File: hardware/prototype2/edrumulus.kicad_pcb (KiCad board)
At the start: 2 copper layers, 82 parts, among them J1 NMJ6HCD2, J10 DIN-5, J2 NMJ6HCD2, J3 NMJ6HCD2, J4 NMJ6HCD2, J5 NMJ6HCD2, J6 NMJ6HCD2, J7 NMJ6HCD2, J8 NMJ6HCD2, J9 NMJ6HCD2, U1 ESP32-DEVKIT-V1, U2 6N138

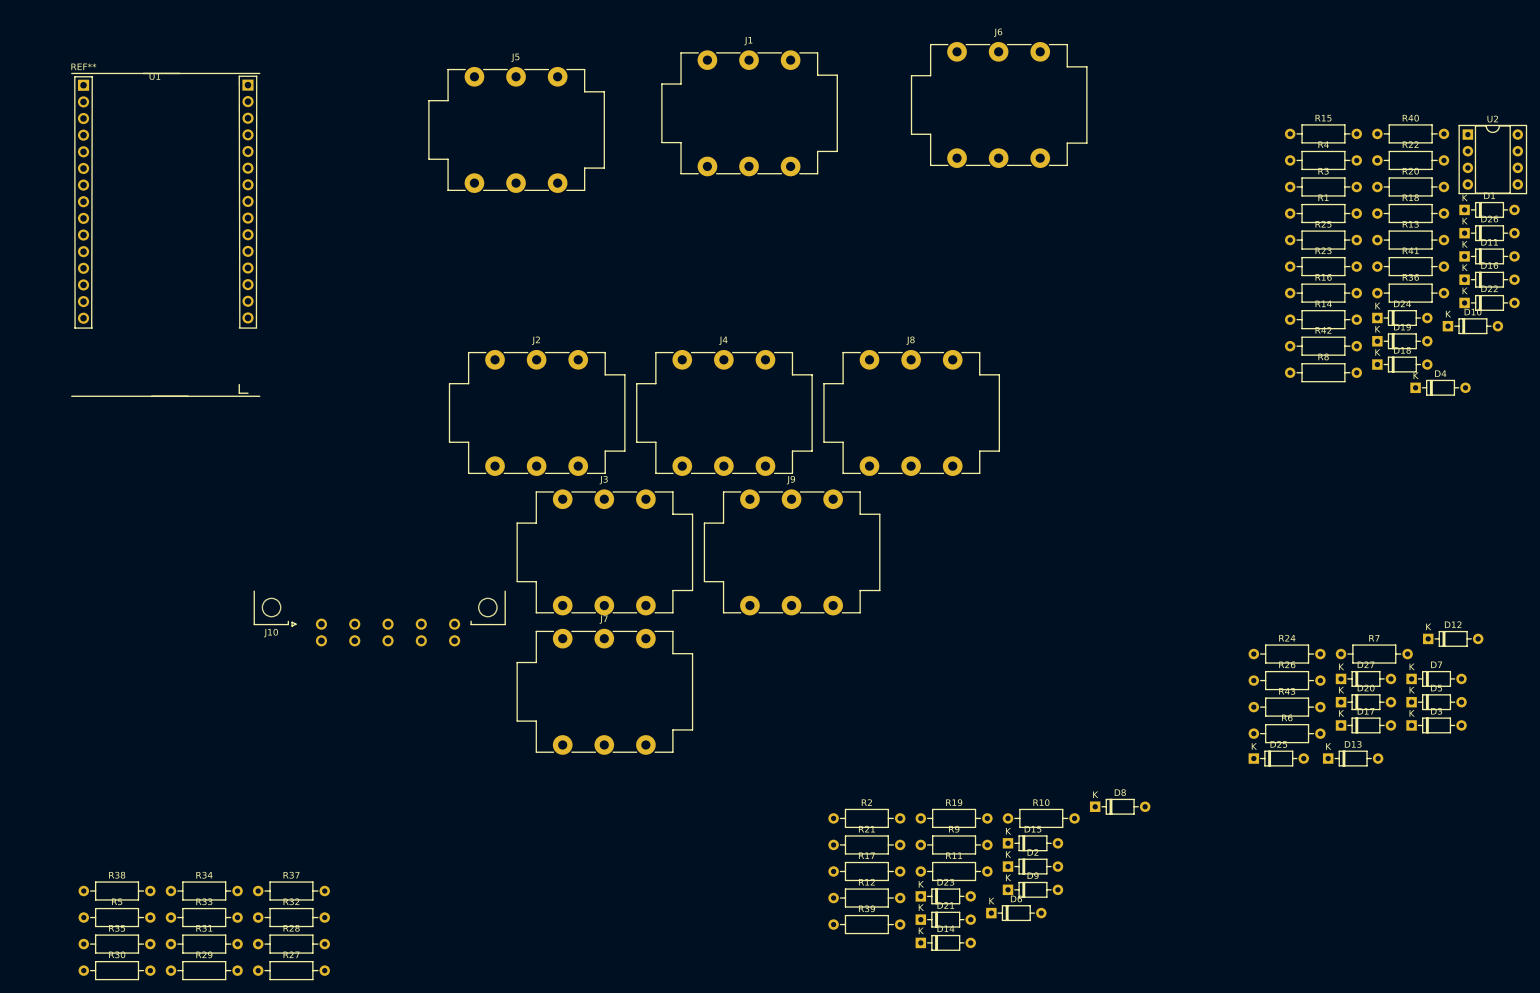
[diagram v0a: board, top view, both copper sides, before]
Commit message: fix bug with MIDI IN/OUT
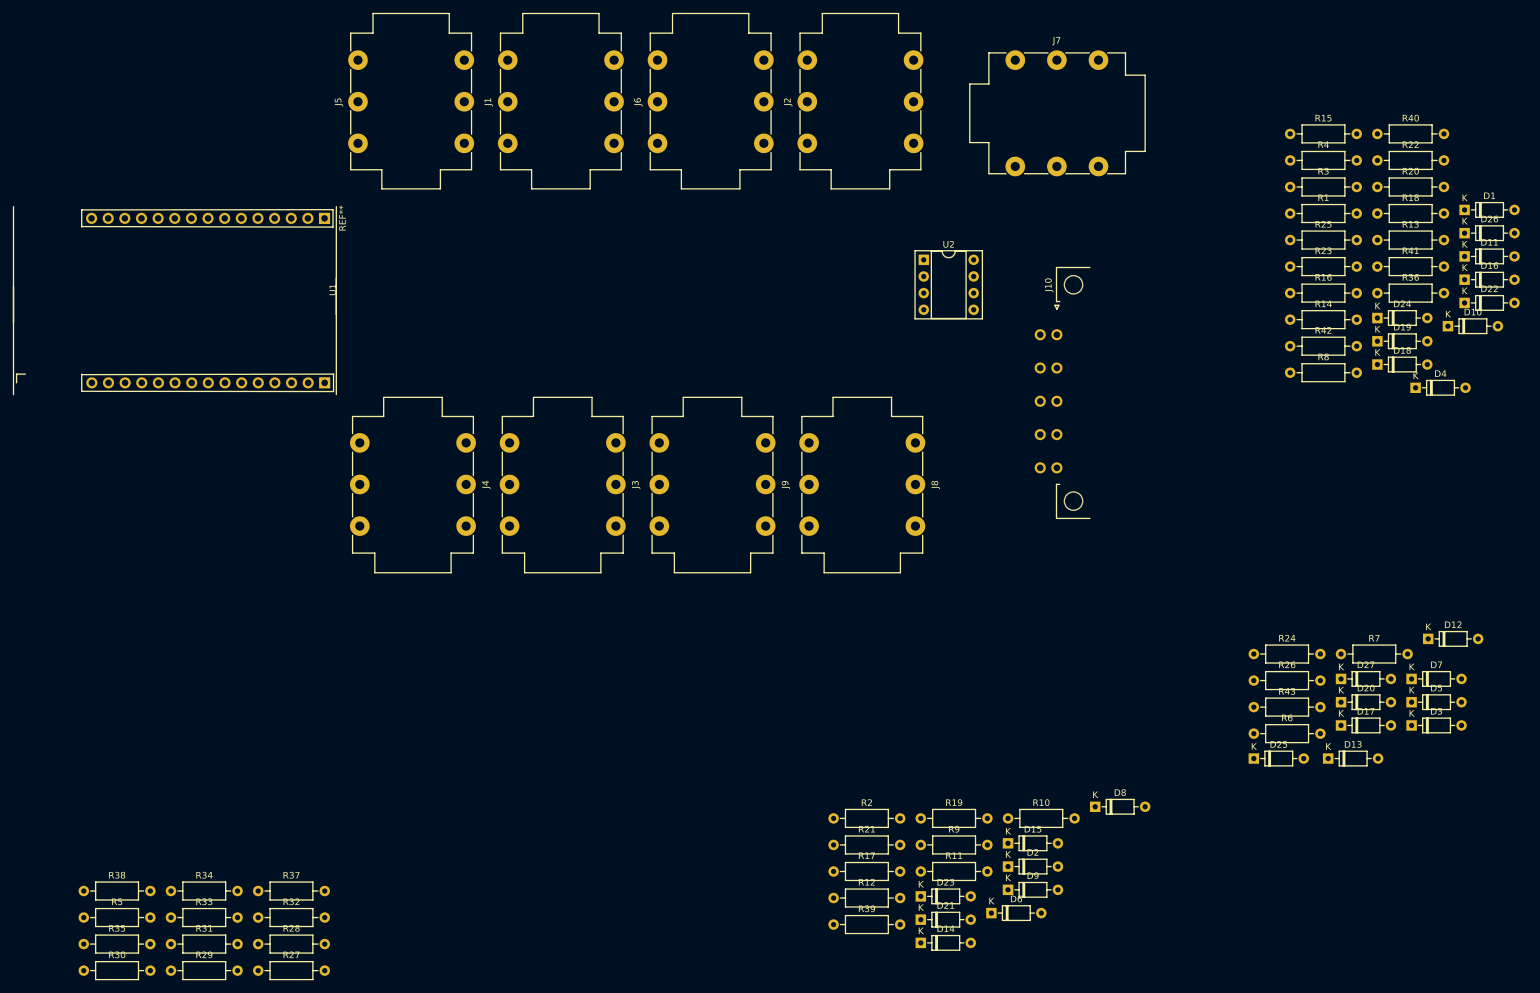
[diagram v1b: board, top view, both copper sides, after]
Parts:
- moved J10 123.9 mm to (194.3, 69.8), turned to 270 degrees
- moved J7 112.1 mm to (188.0, 30.5)
- moved U2 85.2 mm to (174.0, 61.0)
- moved J2 58.0 mm to (156.2, 43.2), turned to 90 degrees
- moved J6 47.8 mm to (133.3, 43.2), turned to 90 degrees
- moved U1 42.1 mm to (82.5, 54.6), turned to 270 degrees
- moved J4 35.3 mm to (104.1, 88.9), turned to 270 degrees
- moved J1 33.0 mm to (110.5, 43.2), turned to 90 degrees
- moved J5 20.5 mm to (87.6, 43.2), turned to 90 degrees
- moved J8 14.5 mm to (172.7, 88.9), turned to 270 degrees
- moved J3 11.8 mm to (127.0, 88.9), turned to 270 degrees
- moved J9 8.93 mm to (149.9, 88.9), turned to 270 degrees

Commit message: some updated to PCB
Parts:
- added J11: DIN-5, Connector_DIN:DIN41612_B3_2x5_Horizontal, F.Cu at (208.3, 74.9)
- moved J10 40.6 mm to (208.3, 31.8)
- moved U2 22.2 mm to (185.4, 80.0)
- moved J7 15.5 mm to (179.1, 43.2), turned to 90 degrees
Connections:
- R39 pad 1: Net-(J10-Pad4) -> Net-(D27-Pad1)
- R39 pad 2: Net-(D27-Pad1) -> Net-(J10-Pad4)
- R41 pad 1: UART_TX -> Net-(J11-Pad5)
- R41 pad 2: Net-(J10-Pad2) -> UART_TX

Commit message: reorder jack sockets
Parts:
- J1: value NMJ6HCD2 -> Snare
- J2: value NMJ6HCD2 -> Hi-Hat
- J3: value NMJ6HCD2 -> Crash
- J4: value NMJ6HCD2 -> Ride
- J5: value NMJ6HCD2 -> Kick
- J6: value NMJ6HCD2 -> Tom1
- J7: value NMJ6HCD2 -> Tom2
- J8: value NMJ6HCD2 -> Tom3
- J9: value NMJ6HCD2 -> Hi-Hat Ctrl
- moved J6 49.8 mm to (149.9, 90.2), turned to 270 degrees
- moved J7 47.4 mm to (172.7, 90.2), turned to 270 degrees
- moved J9 46.2 mm to (156.2, 43.2), turned to 90 degrees
- moved U2 42.4 mm to (191.8, 38.1), turned to 180 degrees
- moved J8 22.9 mm to (195.6, 90.2)
- moved J3 22.9 mm to (104.1, 90.2)
- moved J4 22.9 mm to (127.0, 90.2)
- moved J2 22.9 mm to (133.3, 43.2)
- moved J1 22.9 mm to (87.6, 43.2)
- moved J5 22.9 mm to (110.5, 43.2)

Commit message: some tests, moving components
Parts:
- moved R38 167.5 mm to (179.1, 55.9), turned to 180 degrees
- moved R28 151.3 mm to (195.6, 77.5), turned to 90 degrees
- moved R39 137.6 mm to (199.4, 30.5), turned to 270 degrees
- moved R12 136.4 mm to (64.8, 61.0)
- moved R27 136.1 mm to (172.7, 77.5), turned to 90 degrees
- moved R31 135.0 mm to (54.6, 30.5)
- moved R30 132.7 mm to (77.5, 40.6), turned to 90 degrees
- moved R10 132.3 mm to (91.4, 54.6)
- moved R37 130.0 mm to (153.7, 55.9)
- moved R29 129.4 mm to (71.1, 40.6), turned to 90 degrees
- moved R11 125.3 mm to (91.4, 59.7)
- moved R21 114.6 mm to (76.2, 72.4)
- moved R35 104.4 mm to (44.5, 61.0)
- moved R17 101.3 mm to (184.2, 55.9)
- moved R5 101.1 mm to (104.1, 78.7), turned to 180 degrees
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
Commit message: small fixes
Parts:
- removed J10, J11: DIN-5, Connector_DIN:DIN41612_B3_2x5_Horizontal

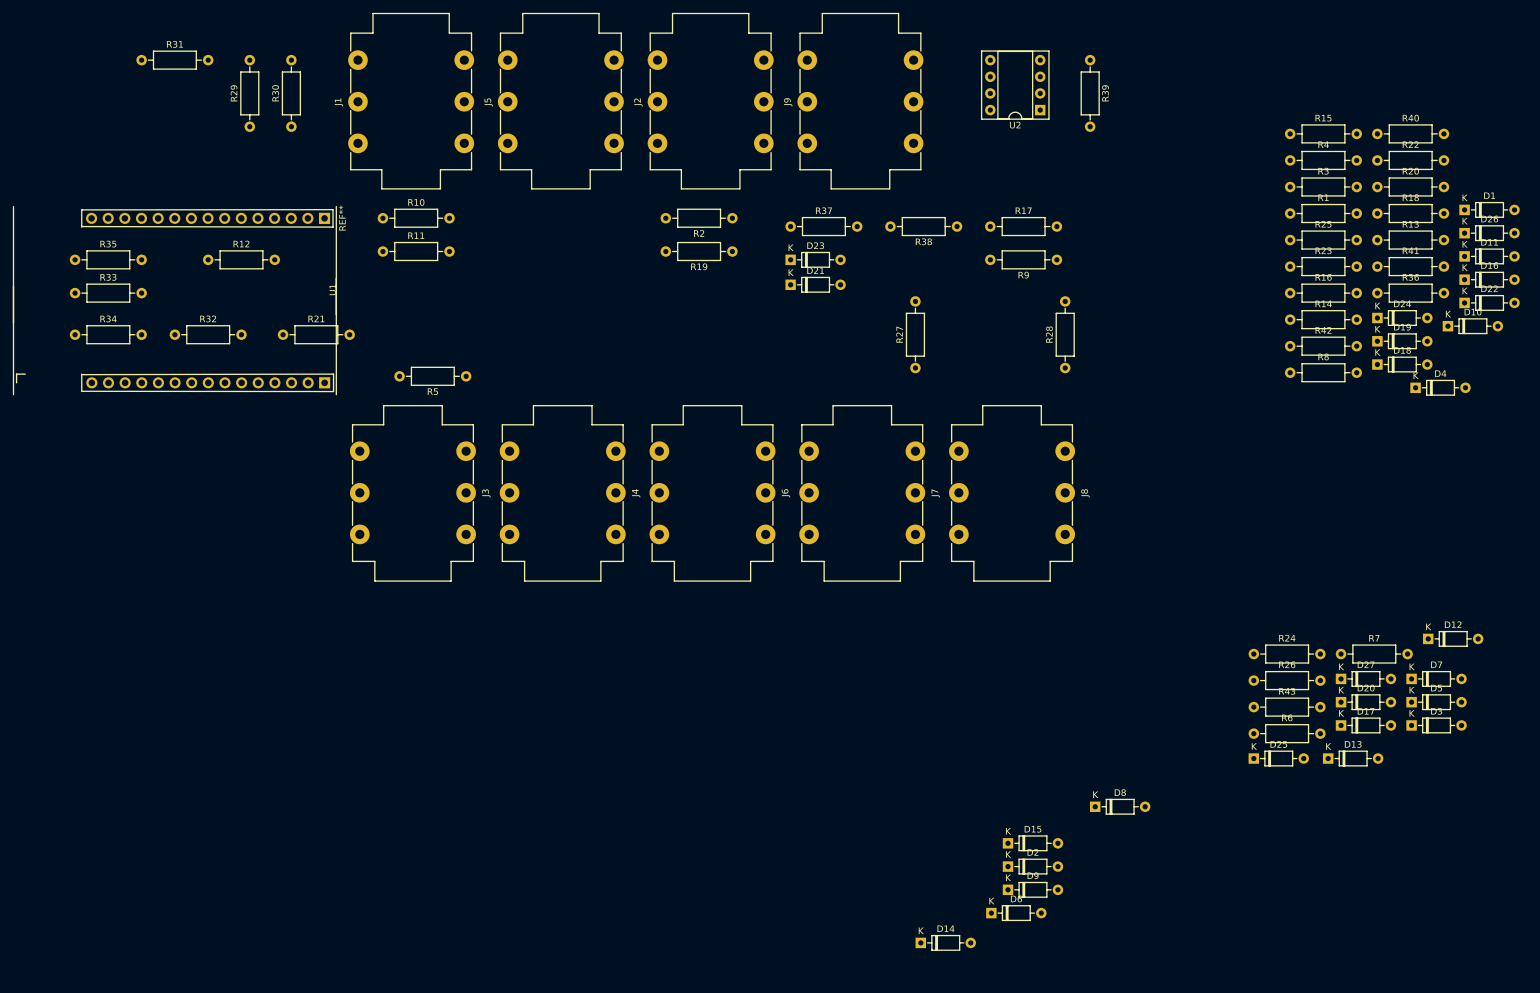
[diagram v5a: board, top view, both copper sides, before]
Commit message: clean up schematics -> PCB must be re-started from scratch
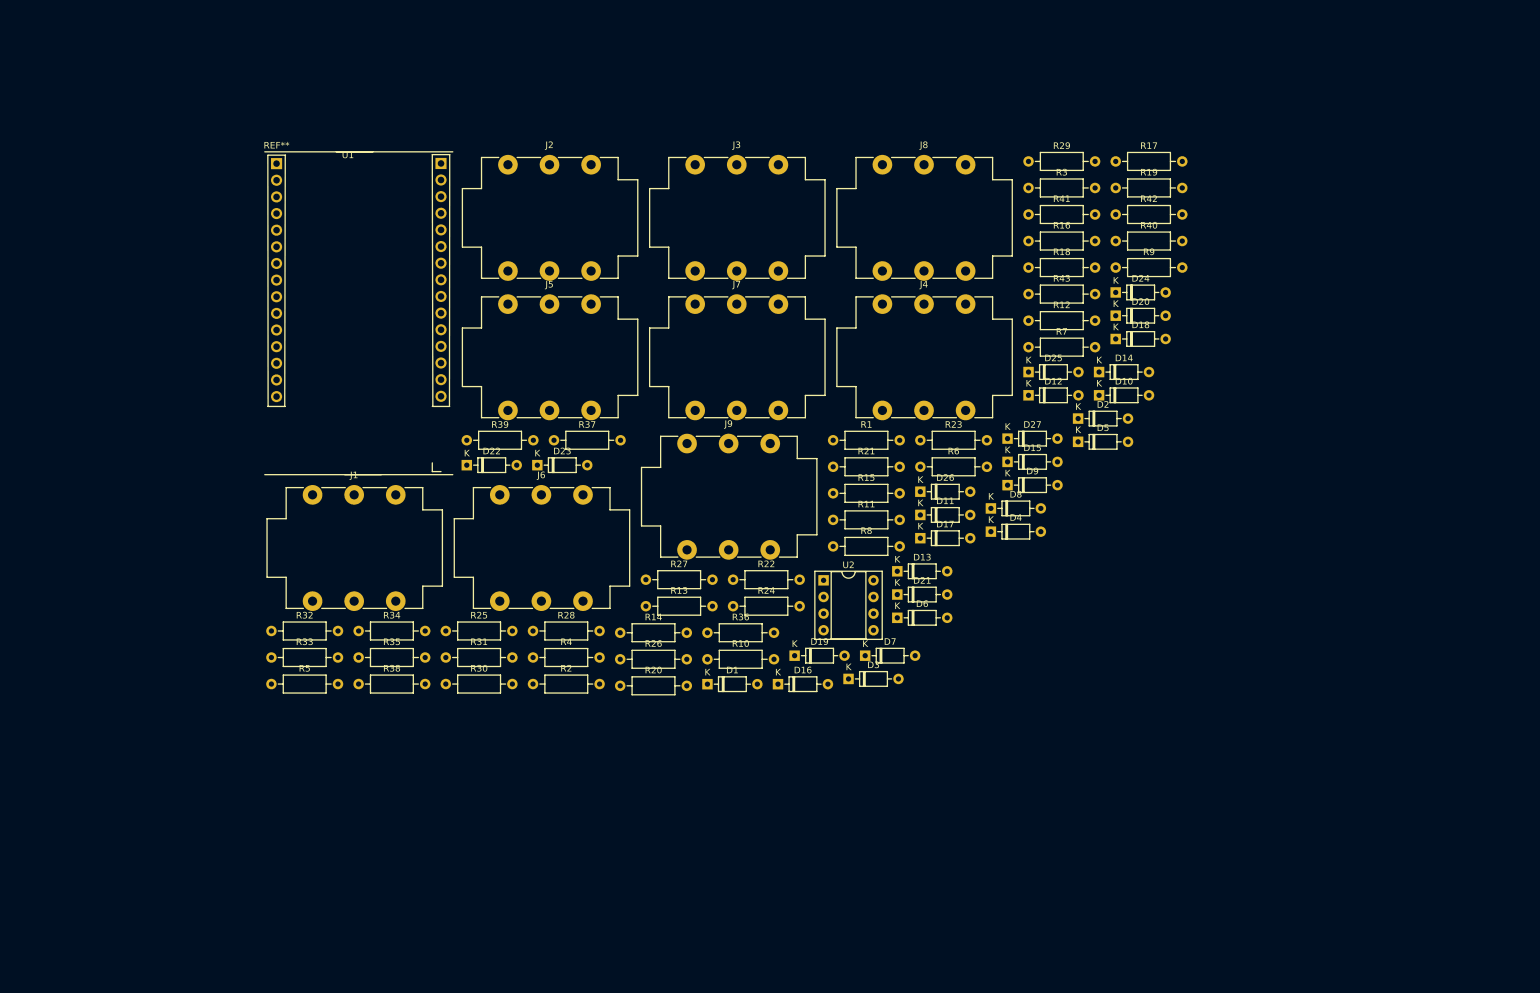
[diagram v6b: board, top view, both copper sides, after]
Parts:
- J2: value Hi-Hat -> Snare
- J3: value Crash -> Snare
- J4: value Ride -> Snare
- J6: value Tom1 -> Kick
- J7: value Tom2 -> Kick
- J8: value Tom3 -> Kick
- moved D22 154.3 mm to (104.2, 92.3)
- moved R25 142.0 mm to (101.0, 117.6)
- moved R20 138.4 mm to (127.7, 126.0)
- moved R4 138.2 mm to (114.3, 121.7)
- moved D1 136.4 mm to (141.0, 125.7)
- moved R12 125.6 mm to (190.0, 70.2)
- moved R13 124.9 mm to (131.6, 113.8)
- moved D16 121.6 mm to (151.7, 125.7)
- moved R29 119.0 mm to (190.0, 45.9), turned to 0 degrees
- moved R22 117.3 mm to (144.9, 109.8)
- moved R38 115.0 mm to (87.7, 125.7), turned to 0 degrees
- moved R36 114.6 mm to (141.0, 117.9)
- moved R14 112.9 mm to (127.7, 117.9)
- moved R39 111.4 mm to (104.2, 88.5), turned to 0 degrees
- moved R31 102.3 mm to (101.0, 121.7)
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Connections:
- D18 pad 1: GPIO39 -> GPIO15
- D19 pad 1: GPIO12 -> GPIO39
- D20 pad 1: GPIO15 -> GPIO12
- D22 pad 2: GPIO39 -> GPIO15
- D23 pad 2: GPIO12 -> GPIO39
- D24 pad 2: GPIO15 -> GPIO12
- R26 pad 2: GPIO39 -> GPIO15
- R27 pad 2: GPIO12 -> GPIO39
- R28 pad 2: GPIO15 -> GPIO12
- R30 pad 1: GPIO39 -> GPIO15
- R31 pad 1: GPIO12 -> GPIO39
- R32 pad 1: GPIO15 -> GPIO12
- R34 pad 2: GPIO39 -> GPIO15
- R35 pad 2: GPIO12 -> GPIO39
- R36 pad 2: GPIO15 -> GPIO12

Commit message: bug fix with audio jack connector names
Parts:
- J2: value Snare -> Hi-Hat
- J3: value Snare -> Crash
- J4: value Snare -> Ride
- J6: value Kick -> Tom3
- J7: value Kick -> Tom1
- J8: value Kick -> Tom2
